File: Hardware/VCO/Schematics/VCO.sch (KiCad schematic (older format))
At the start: 12 parts

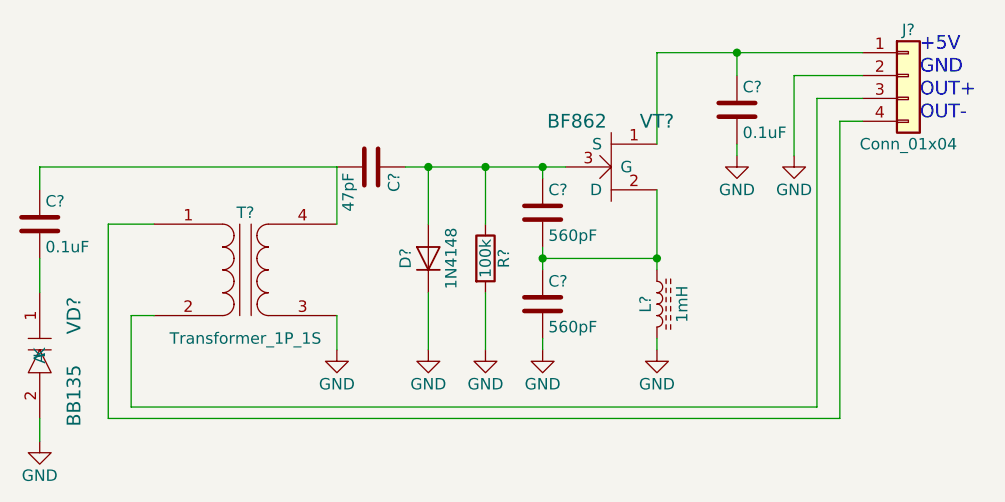
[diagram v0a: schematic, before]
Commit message: Fixed incorrectly-connected VT1
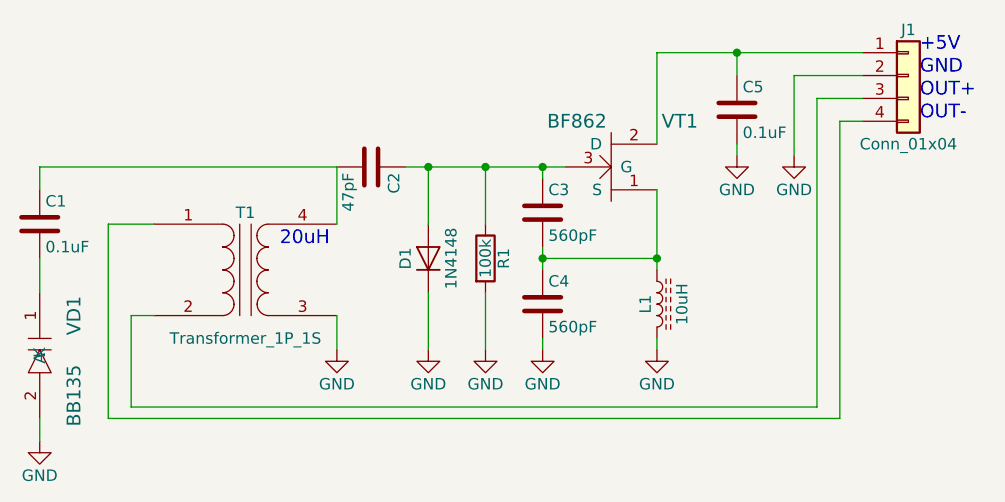
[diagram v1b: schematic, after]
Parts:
- L1: renamed from L?; value 1mH -> 10uH
- gave numbers to parts that had none: 11
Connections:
- net at C5.1, J1.1 (Pin_1): now also VT1.2 (D); no longer VT1.1 (S)
- net at C3.2, C4.1, L1.1: now also VT1.1 (S); no longer VT1.2 (D)
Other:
- note added: "20uH"
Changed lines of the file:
@@
 $EndDescr
 $Comp
-L Conn_01x04 J?
+L Conn_01x04 J1
 U 1 1 5B7063C4
 P 5650 1450
-F 0 "J?" H 5650 1650 50  0000 C CNN
+F 0 "J1" H 5650 1650 50  0000 C CNN
 F 1 "Conn_01x04" H 5650 1150 50  0000 C CNN
 F 2 "" H 5650 1450 50  0001 C CNN
@@
 OUT-
 $Comp
-L GND #PWR?
+L GND #PWR8
 U 1 1 5B706542
 P 5150 1800
-F 0 "#PWR?" H 5150 1550 50  0001 C CNN
+F 0 "#PWR8" H 5150 1550 50  0001 C CNN
 F 1 "GND" H 5150 1650 50  0000 C CNN
 F 2 "" H 5150 1800 50  0001 C CNN
@@
 $EndComp
 $Comp
-L C C?
+L C C5
 U 1 1 5B70657A
 P 4900 1600
-F 0 "C?" H 4925 1700 50  0000 L CNN
+F 0 "C5" H 4925 1700 50  0000 L CNN
 F 1 "0.1uF" H 4925 1500 50  0000 L CNN
 F 2 "" H 4938 1450 50  0001 C CNN
@@
 $EndComp
 $Comp
-L GND #PWR?
+L GND #PWR7
 U 1 1 5B706662
 P 4900 1800
-F 0 "#PWR?" H 4900 1550 50  0001 C CNN
+F 0 "#PWR7" H 4900 1550 50  0001 C CNN
 F 1 "GND" H 4900 1650 50  0000 C CNN
 F 2 "" H 4900 1800 50  0001 C CNN
@@
 $EndComp
 $Comp
-L BF862 VT?
+L BF862 VT1
 U 1 1 5B706795
-P 4400 1650
-F 0 "VT?" H 4550 1650 60  0000 C CNN
+P 4400 2050
+F 0 "VT1" H 4650 1650 60  0000 C CNN
 F 1 "BF862" H 4200 1650 60  0000 C CNN
-F 2 "" H 4400 1650 60  0001 C CNN
-F 3 "" H 4400 1650 60  0001 C CNN
-	1    4400 1650
-	1    0    0    -1
-$EndComp
-$Comp
-L L_Core_Ferrite L?
+F 2 "" H 4400 2050 60  0001 C CNN
+F 3 "" H 4400 2050 60  0001 C CNN
+	1    4400 2050
+	1    0    0    1
+$EndComp
+$Comp
+L L_Core_Ferrite L1
 U 1 1 5B7068F5
 P 4550 2450
-F 0 "L?" V 4500 2450 50  0000 C CNN
-F 1 "1mH" V 4660 2450 50  0000 C CNN
+F 0 "L1" V 4500 2450 50  0000 C CNN
+F 1 "10uH" V 4660 2450 50  0000 C CNN
 F 2 "" H 4550 2450 50  0001 C CNN
 F 3 "" H 4550 2450 50  0001 C CNN
@@
 $EndComp
 $Comp
-L GND #PWR?
+L GND #PWR6
 U 1 1 5B7069A3
 P 4550 2650
-F 0 "#PWR?" H 4550 2400 50  0001 C CNN
+F 0 "#PWR6" H 4550 2400 50  0001 C CNN
 F 1 "GND" H 4550 2500 50  0000 C CNN
 F 2 "" H 4550 2650 50  0001 C CNN
@@
 $EndComp
 $Comp
-L C C?
+L C C3
 U 1 1 5B706A22
 P 4050 2050
-F 0 "C?" H 4075 2150 50  0000 L CNN
+F 0 "C3" H 4075 2150 50  0000 L CNN
 F 1 "560pF" H 4075 1950 50  0000 L CNN
 F 2 "" H 4088 1900 50  0001 C CNN
@@
 $EndComp
 $Comp
-L C C?
+L C C4
 U 1 1 5B706AA9
 P 4050 2450
-F 0 "C?" H 4075 2550 50  0000 L CNN
+F 0 "C4" H 4075 2550 50  0000 L CNN
 F 1 "560pF" H 4075 2350 50  0000 L CNN
 F 2 "" H 4088 2300 50  0001 C CNN
@@
 $EndComp
 $Comp
-L GND #PWR?
+L GND #PWR5
 U 1 1 5B706B54
 P 4050 2650
-F 0 "#PWR?" H 4050 2400 50  0001 C CNN
+F 0 "#PWR5" H 4050 2400 50  0001 C CNN
 F 1 "GND" H 4050 2500 50  0000 C CNN
 F 2 "" H 4050 2650 50  0001 C CNN
@@
 $EndComp
 $Comp
-L R R?
+L R R1
 U 1 1 5B706C78
 P 3800 2250
-F 0 "R?" V 3880 2250 50  0000 C CNN
+F 0 "R1" V 3880 2250 50  0000 C CNN
 F 1 "100k" V 3800 2250 50  0000 C CNN
 F 2 "" V 3730 2250 50  0001 C CNN
@@
 $EndComp
 $Comp
-L GND #PWR?
+L GND #PWR4
 U 1 1 5B706D03
 P 3800 2650
-F 0 "#PWR?" H 3800 2400 50  0001 C CNN
+F 0 "#PWR4" H 3800 2400 50  0001 C CNN
 F 1 "GND" H 3800 2500 50  0000 C CNN
 F 2 "" H 3800 2650 50  0001 C CNN
@@
 $EndComp
 $Comp
-L D D?
+L D D1
 U 1 1 5B7071A6
 P 3550 2250
-F 0 "D?" H 3550 2350 50  0000 C CNN
+F 0 "D1" H 3550 2350 50  0000 C CNN
 F 1 "1N4148" H 3550 2150 50  0000 C CNN
 F 2 "" H 3550 2250 50  0001 C CNN
@@
 $EndComp
 $Comp
-L GND #PWR?
+L GND #PWR3
 U 1 1 5B707304
 P 3550 2650
-F 0 "#PWR?" H 3550 2400 50  0001 C CNN
+F 0 "#PWR3" H 3550 2400 50  0001 C CNN
 F 1 "GND" H 3550 2500 50  0000 C CNN
 F 2 "" H 3550 2650 50  0001 C CNN
@@
 $EndComp
 $Comp
-L C C?
+L C C2
 U 1 1 5B707492
 P 3300 1850
-F 0 "C?" H 3325 1950 50  0000 L CNN
+F 0 "C2" H 3325 1950 50  0000 L CNN
 F 1 "47pF" H 3325 1750 50  0000 L CNN
 F 2 "" H 3338 1700 50  0001 C CNN
@@
 $EndComp
 $Comp
-L Transformer_1P_1S T?
+L Transformer_1P_1S T1
 U 1 1 5B7075E9
 P 2750 2300
-F 0 "T?" H 2750 2550 50  0000 C CNN
+F 0 "T1" H 2750 2550 50  0000 C CNN
 F 1 "Transformer_1P_1S" H 2750 2000 50  0000 C CNN
 F 2 "" H 2750 2300 50  0001 C CNN
@@
 $EndComp
 $Comp
-L GND #PWR?
+L GND #PWR2
 U 1 1 5B707677
 P 3150 2650
-F 0 "#PWR?" H 3150 2400 50  0001 C CNN
+F 0 "#PWR2" H 3150 2400 50  0001 C CNN
 F 1 "GND" H 3150 2500 50  0000 C CNN
 F 2 "" H 3150 2650 50  0001 C CNN
@@
 	1850 1850 1850 1950
 $Comp
-L C C?
+L C C1
 U 1 1 5B7077BD
 P 1850 2100
-F 0 "C?" H 1875 2200 50  0000 L CNN
+F 0 "C1" H 1875 2200 50  0000 L CNN
 F 1 "0.1uF" H 1875 2000 50  0000 L CNN
 F 2 "" H 1888 1950 50  0001 C CNN
@@
 $EndComp
 $Comp
-L BB135 VD?
+L BB135 VD1
 U 1 1 5B707DE6
 P 1900 2650
-F 0 "VD?" H 1750 2750 60  0000 C CNN
+F 0 "VD1" H 1750 2750 60  0000 C CNN
 F 1 "BB135" H 2100 2750 60  0000 C CNN
 F 2 "" H 1950 2700 60  0001 C CNN
@@
 	1850 2400 1850 2250
 $Comp
-L GND #PWR?
+L GND #PWR1
 U 1 1 5B707F0D
 P 1850 3050
-F 0 "#PWR?" H 1850 2800 50  0001 C CNN
+F 0 "#PWR1" H 1850 2800 50  0001 C CNN
 F 1 "GND" H 1850 2900 50  0000 C CNN
 F 2 "" H 1850 3050 50  0001 C CNN
@@
 Wire Wire Line
 	1850 3050 1850 2950
+Text Notes 2900 2200 0    60   ~ 0
+20uH
 $EndSCHEMATC

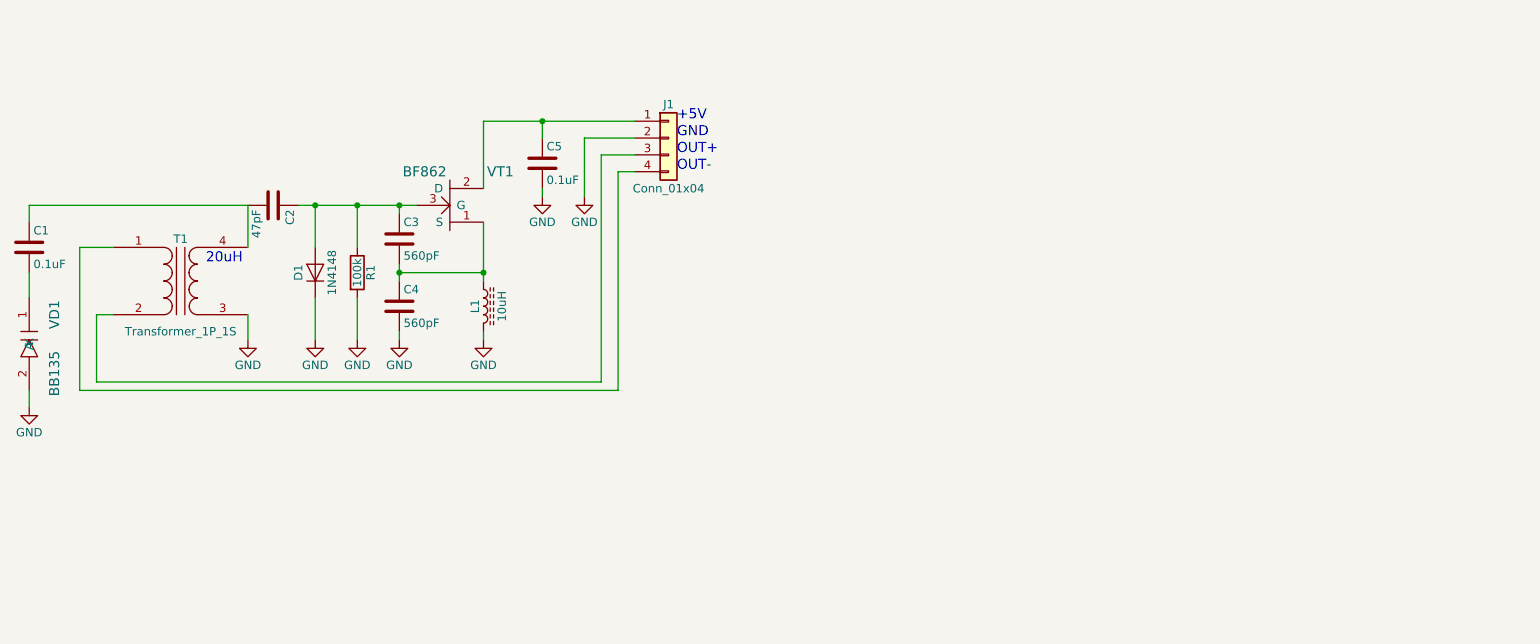
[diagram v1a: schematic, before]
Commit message: Preliminary VCO schematic with tuning and buffer amplifier.
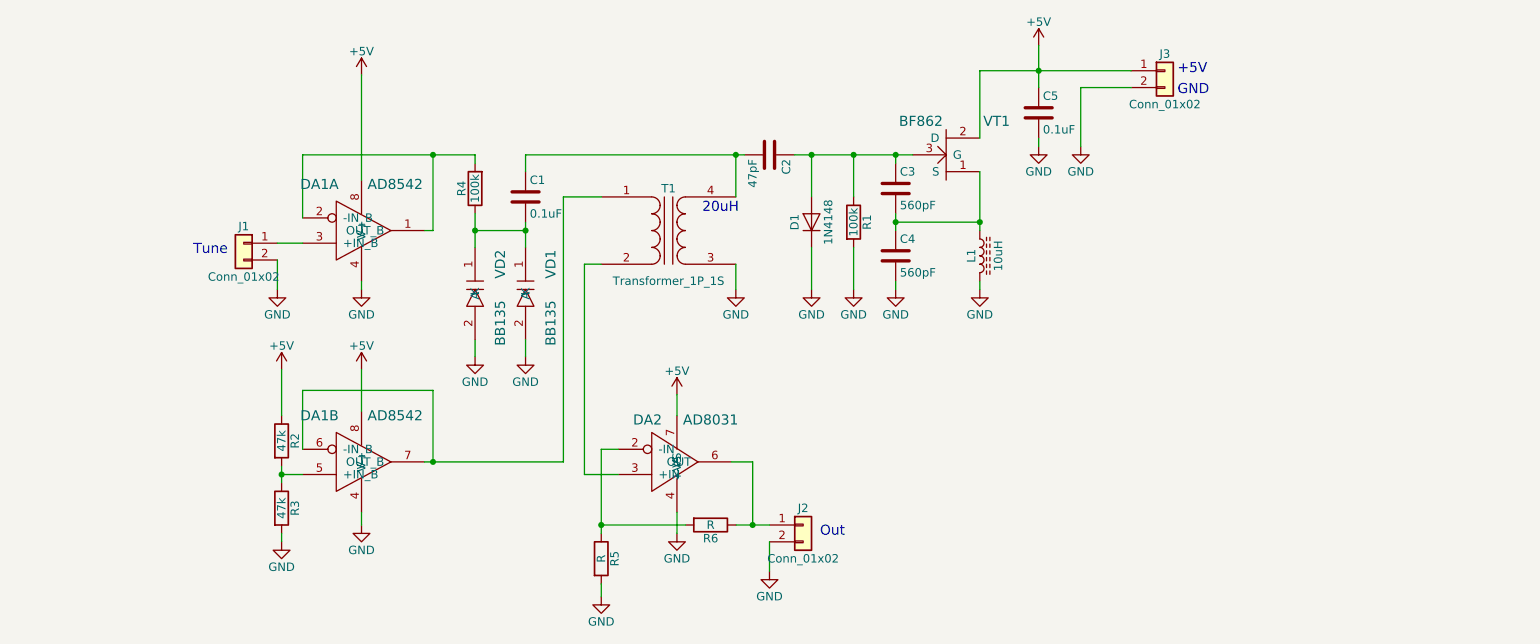
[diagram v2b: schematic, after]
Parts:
- removed J1: Conn_01x04, symbol Conn_01x04
- added DA1: AD8542, symbol AD8542
- added DA2: AD8031, symbol AD8031
- added J1, J2, J3: Conn_01x02, symbol Conn_01x02
- added R2, R3: 47k, symbol R
- added R4: 100k, symbol R
- added R5, R6: R, symbol R
- added VD2: BB135, symbol BB135
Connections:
- net GND: now also DA1.4 (V-), DA1.4 (V-), DA2.4 (-VS), J1.2 (Pin_2), J2.2 (Pin_2), J3.2 (Pin_2), R3.2, R5.2, VD2.2 (A)
- net +5V: now reaches C5.1, VT1.2 (D)
- net +5V: now also DA1.8 (V+), DA1.8 (V+), DA2.7 (+VS), J3.1 (Pin_1), R2.1
- net at T1.2 (AB): now also DA2.3 (+IN)
- net at T1.1 (AA): now also DA1.6 (-IN_B), DA1.7 (OUT_B)
- net at C1.2, VD1.1 (K): now also R4.1, VD2.1 (K)
- new net: DA1.1 (OUT_B), DA1.2 (-IN_B), R4.2
- new net: DA1.3 (+IN_B), J1.1 (Pin_1)
- new net: DA1.5 (+IN_B), R2.2, R3.1
- new net: DA2.2 (-IN), R5.1, R6.2
- new net: DA2.6 (OUT), J2.1 (Pin_1), R6.1
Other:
- note added: "Out"
- note added: "Tune"
- note removed: "OUT+"
- note removed: "OUT-"
- moved on the sheet: C1, C2, C3, C4, C5, D1, L1, R1, T1, VD1, VT1

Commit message: -Simpler (and working) VCO with good sinusoidal output.
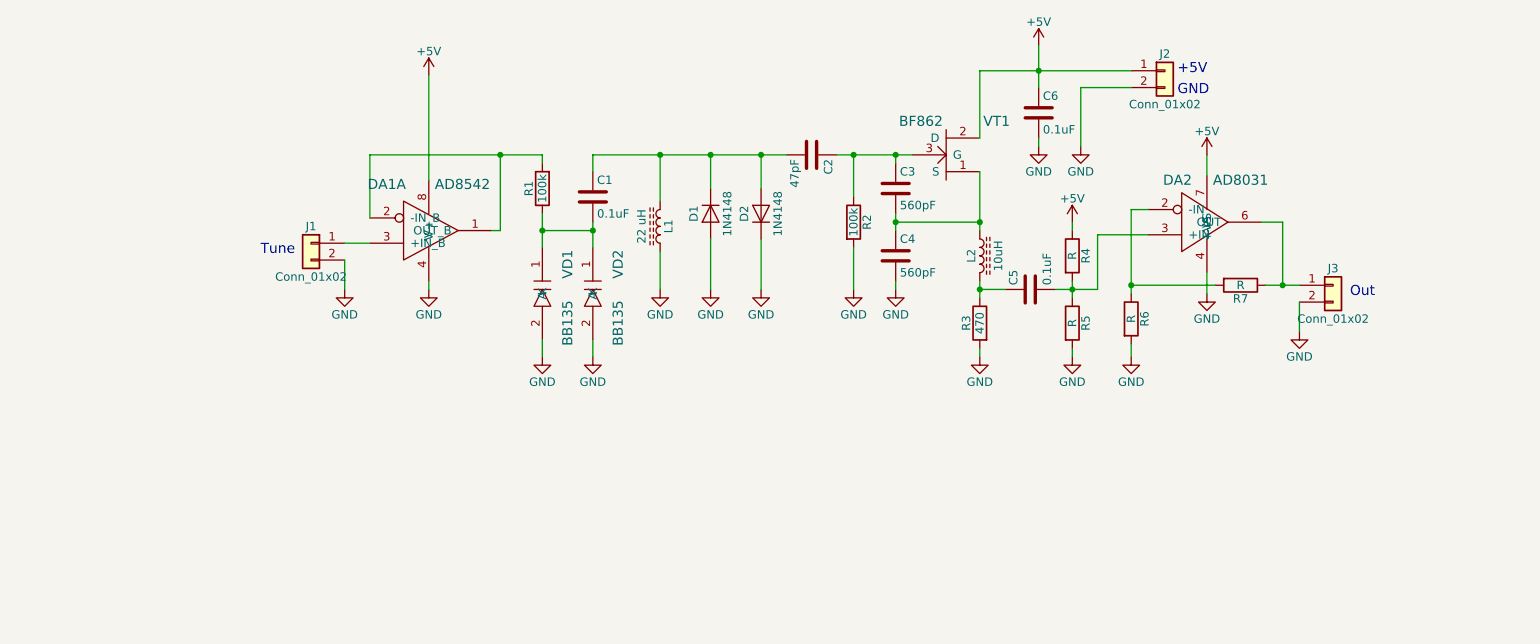
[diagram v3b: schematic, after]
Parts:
- removed unit 2 of DA1
- removed R2: 47k, symbol R
- removed T1: Transformer_1P_1S, symbol Transformer_1P_1S
- added C5: 0.1uF, symbol C
- added D2: 1N4148, symbol D
- added L1: 22 uH, symbol L_Core_Ferrite
- added R4, R5: R, symbol R
- R3: value 47k -> 470
- renumbered C5 to C6, J3 to J2, J2 to J3, L1 to L2, R4 to R1, R1 to R2, R5 to R6, R6 to R7, VD2 to VD1, VD1 to VD2
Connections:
- net +5V: now also R4.1
- net GND: now also D1.2 (A), D2.1 (K), L1.2, R5.2; no longer D1.1 (K), L2.2
- net at C2.1, C3.1, R2.1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: no longer D1.2 (A)
- net at C1.1, C2.2: now also D1.1 (K), D2.2 (A), L1.1
- net at DA2.3 (+IN): now also C5.2, R4.2, R5.1
- net at R3.1: now also L2.2, C5.1
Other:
- note removed: "20uH"
- moved on the sheet: C1, C2, DA1A, DA2, J1, J3, R1, R6, R7, VD1, VD2

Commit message: Actually generating with this sceme
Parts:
- L1: value 22 uH -> 27 uH
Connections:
- net GND: no longer C4.2
- net at C5.1, L2.2, R3.1: now also C4.2
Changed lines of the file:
@@
-$EndComp
-$Comp
-L GND #PWR10
-U 1 1 5B706B54
-P 7000 2350
-F 0 "#PWR10" H 7000 2100 50  0001 C CNN
-F 1 "GND" H 7000 2200 50  0000 C CNN
-F 2 "" H 7000 2350 50  0001 C CNN
-F 3 "" H 7000 2350 50  0001 C CNN
-	1    7000 2350
-	1    0    0    -1
 $EndComp
 $Comp
@@
 Wire Wire Line
 	7000 1600 7000 1550
-Wire Wire Line
-	7000 2300 7000 2350
 Connection ~ 7000 1550
 Wire Wire Line
@@
 Connection ~ 7500 2350
 Wire Wire Line
-	7650 2350 7500 2350
+	7000 2350 7650 2350
 Wire Wire Line
 	8050 2300 8050 2400
@@
 P 5600 1975
 F 0 "L1" V 5550 1975 50  0000 C CNN
-F 1 "22 uH" V 5710 1975 50  0000 C CNN
+F 1 "27 uH" V 5710 1975 50  0000 C CNN
 F 2 "" H 5600 1975 50  0001 C CNN
 F 3 "" H 5600 1975 50  0001 C CNN
@@
 	-1   0    0    -1
 $EndComp
+Wire Wire Line
+	7000 2300 7000 2350
 $EndSCHEMATC
